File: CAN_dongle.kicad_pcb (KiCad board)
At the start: 2 copper layers, 70 x 70 mm, 77 parts, among them J1 P0-P3, J10 K-LINE, J11 HEADER2X10, J2 JTAG, J3 USB-MINI-A, J4 12V, J5 5V, J6 GND, J7 P4-P7, J8 CAN, J9 TERM, Q1 IRF7313, Q2 IRF7313, Q3 2N7002, Q4 2N7002, U1 LM324, U2 STM32F103CBT6, U3 LM1117, U4 MC34063, U5 MCP2551, X1 XT324

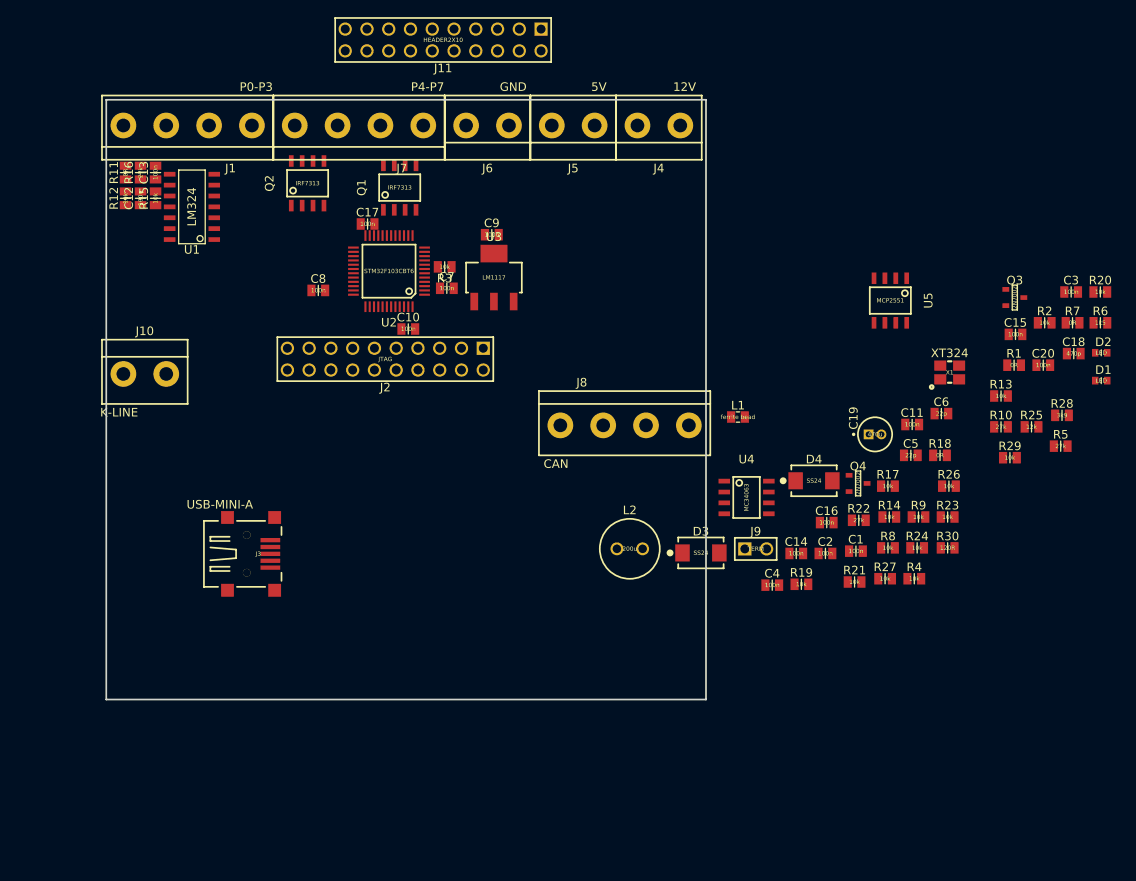
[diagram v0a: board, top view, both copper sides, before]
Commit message: Added LCD, buttons, remapped pins
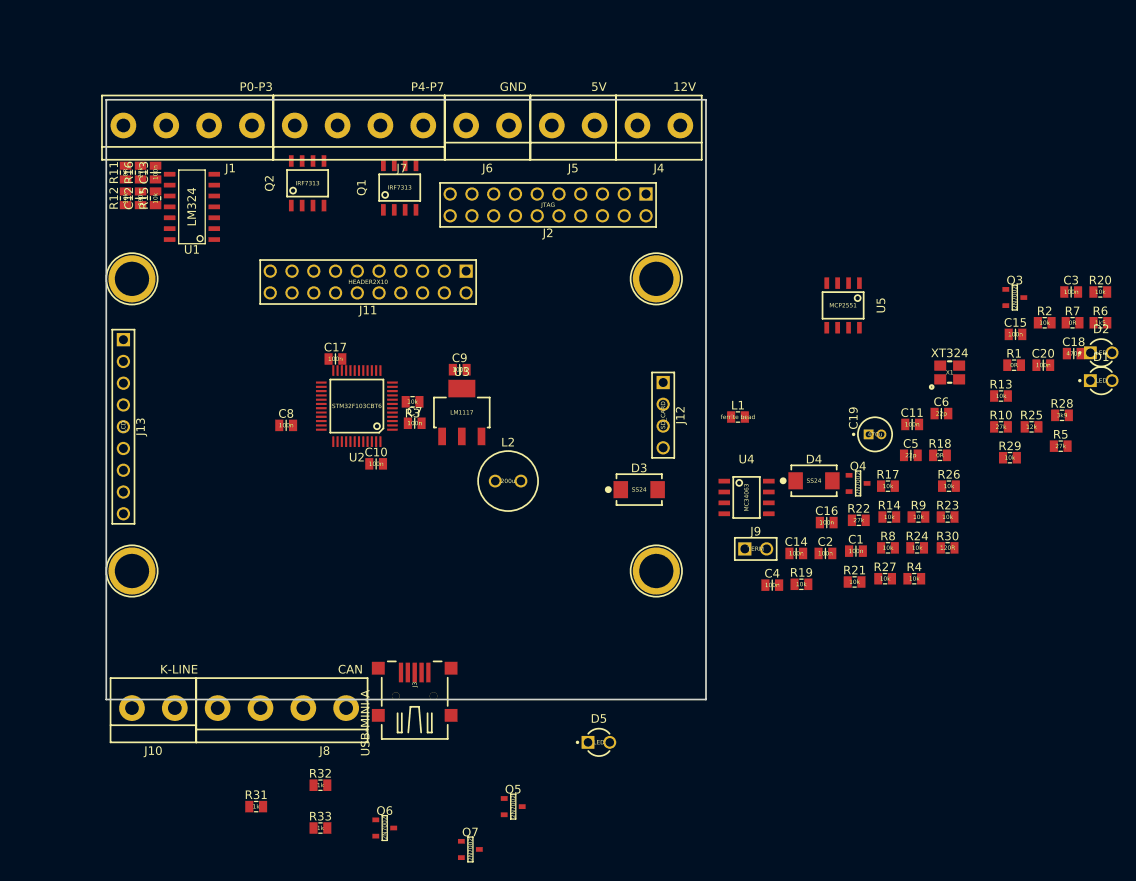
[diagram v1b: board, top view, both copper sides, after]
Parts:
- added D5: LED, z_newlib:LED_3MM, F.Cu at (137.5, 125.0)
- added J12: SD_CARD, z_pinHeaders:HEADER1x4V, F.Cu at (145.0, 83.0)
- added J13: LCD, z_pinHeaders:HEADER1x9V, F.Cu at (82.0, 78.0)
- added J14: LCD_MNTHOLE, z_newlib:MountHole_D4P6, F.Cu at (83.0, 105.0)
- added J15: LCD_MNTHOLE, z_newlib:MountHole_D4P6, F.Cu at (83.0, 70.9)
- added J16: LCD_MNTHOLE, z_newlib:MountHole_D4P6, F.Cu at (144.2, 70.9)
- added J17: LCD_MNTHOLE, z_newlib:MountHole_D4P6, F.Cu at (144.2, 105.0)
- added Q5: 2N7002, z_newlib:SOT23, F.Cu at (127.5, 132.5)
- added Q6: 2N7002, z_newlib:SOT23, F.Cu at (112.5, 135.0)
- added Q7: 2N7002, z_newlib:SOT23, F.Cu at (122.5, 137.5)
- added R31: 1k, z_newlib:R0805, F.Cu at (97.5, 132.5)
- added R32: 1k, z_newlib:R0805, F.Cu at (105.0, 130.0)
- added R33: 1k, z_newlib:R0805, F.Cu at (105.0, 135.0)
- D1, D2: footprint z_newlib:C0603 -> z_newlib:LED_3MM
- R1, R10, R11, R12, R13, R14, R15, R16, R17, R18, R19, R2, R20, R21, R22, R23, R24, R25, R26, R27, R28, R29, R3, R30, R4, R5, R6, R7, R8, R9: footprint z_newlib:C0805 -> z_newlib:R0805
- moved J8 41.4 mm to (108.0, 121.0), turned to 180 degrees
- moved J10 39.5 mm to (88.0, 121.0), turned to 180 degrees
- moved J3 33.3 mm to (116.0, 125.0), turned to 90 degrees
- moved J11 29.6 mm to (122.0, 70.0)
- moved J2 26.2 mm to (143.0, 61.0)
- moved L2 16.3 mm to (126.9, 94.5)
- moved C10 16.2 mm to (111.5, 92.5)
- moved C17 16.2 mm to (106.8, 80.2)
- moved C7 16.2 mm to (116.0, 87.8)
- moved C8 16.2 mm to (101.0, 88.0)
- moved C9 16.2 mm to (121.2, 81.5)
- moved R3 16.2 mm to (115.8, 85.2)
- moved U2 16.2 mm to (109.2, 85.8)
- moved U3 16.2 mm to (121.5, 86.5)
- moved D3 10.3 mm to (142.2, 95.5)
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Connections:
- D1 pad 1: /LED0 -> +3V3
- D1 pad 2: GND -> Net-(D1-Pad2)
- D2 pad 1: /LED1 -> +3V3
- D2 pad 2: GND -> Net-(D2-Pad2)
- J11 pad 2: +15V -> (no net)
- J2 pad 11: Net-(J2-Pad11) -> (no net)
- J2 pad 17: Net-(J2-Pad17) -> (no net)
- J2 pad 19: Net-(J2-Pad19) -> (no net)
- J3 pad 4: Net-(J3-Pad4) -> (no net)
- Q1 pad 2: /P5 -> /P9
- Q1 pad 4: /P4 -> /P8
- Q2 pad 2: /P7 -> /P11
- Q2 pad 4: /P6 -> /P10
- R13 pad 1: /P4 -> /P8
- R14 pad 1: /P5 -> /P9
- R17 pad 1: /P6 -> /P10
- R20 pad 1: /P7 -> /P11
- U2 pad 18: /P8 -> (no net)
- U2 pad 19: /P9 -> (no net)
- U2 pad 20: Net-(U2-Pad20) -> /LCD_D/C
- U2 pad 29: /LED0 -> /P8
- U2 pad 30: /LED1 -> /P9
- U2 pad 41: Net-(U2-Pad41) -> /LCD_LED
- U5 pad 5: Net-(U5-Pad5) -> (no net)

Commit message: Added calculator for ADC buttons. Added input for compression meter. First placement done.
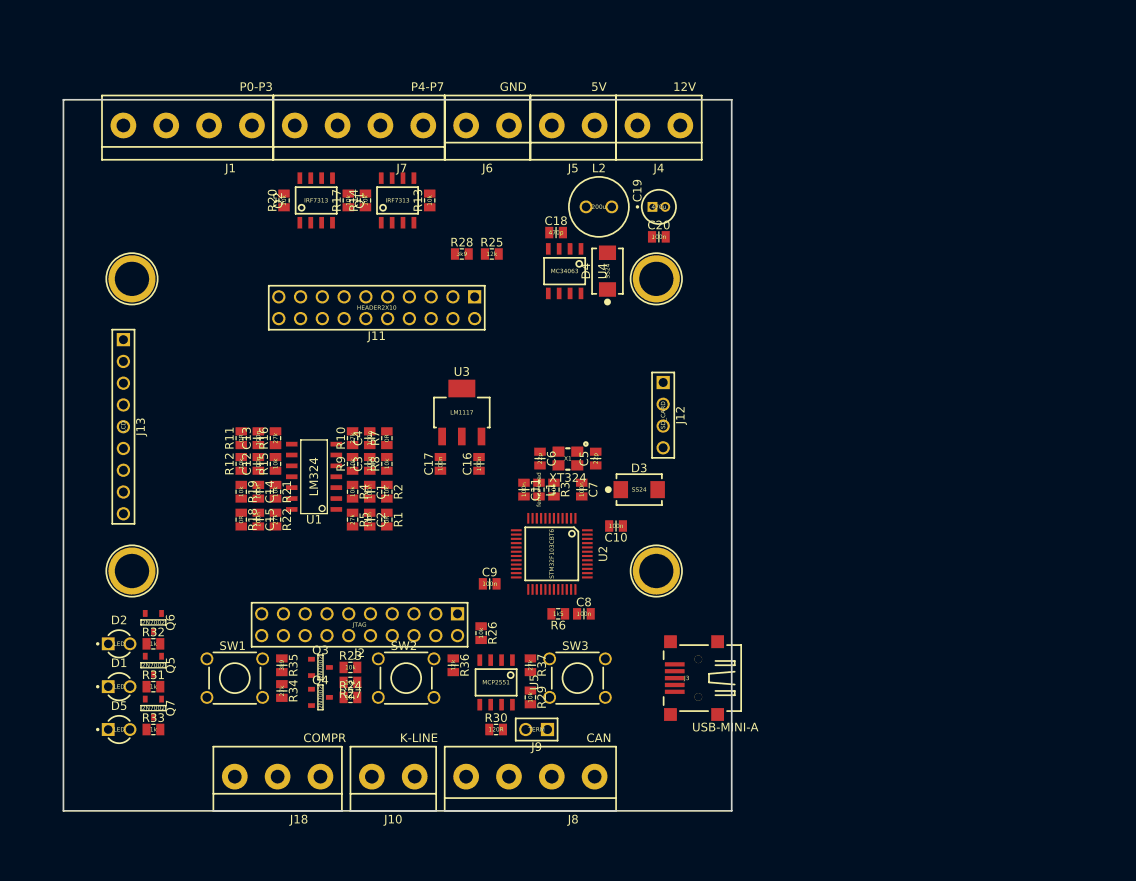
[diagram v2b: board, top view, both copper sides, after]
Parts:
- added J18: COMPR, z_pinHeaders:AK306_LE-3, F.Cu at (105.0, 129.0)
- added R34: 27k, z_newlib:C0805, F.Cu at (100.5, 119.0)
- added R35: 3k9, z_newlib:C0805, F.Cu at (100.5, 116.0)
- added R36: 12k, z_newlib:C0805, F.Cu at (120.5, 116.0)
- added R37: 27k, z_newlib:C0805, F.Cu at (129.5, 116.0)
- added SW1: SWITCH_DUALPINS, z_newlib:TACT_SWITCH_TH_5MM, F.Cu at (95.0, 117.5)
- added SW2: SWITCH_DUALPINS, z_newlib:TACT_SWITCH_TH_5MM, F.Cu at (115.0, 117.5)
- added SW3: SWITCH_DUALPINS, z_newlib:TACT_SWITCH_TH_5MM, F.Cu at (135.0, 117.5)
- moved D1 120.1 mm to (81.5, 118.5)
- moved D2 119.6 mm to (81.5, 113.5)
- moved R20 95.9 mm to (100.8, 61.8), turned to 90 degrees
- moved Q3 91.8 mm to (105.0, 116.2)
- moved C15 91.0 mm to (97.8, 99.0), turned to 270 degrees
- moved C3 84.3 mm to (110.8, 92.5), turned to 90 degrees
- moved R5 83.1 mm to (108.8, 99.0), turned to 270 degrees
- moved R18 81.9 mm to (95.8, 99.0), turned to 270 degrees
- moved R7 81.2 mm to (112.8, 89.5), turned to 90 degrees
- moved R2 79.3 mm to (112.8, 95.8), turned to 270 degrees
- moved R10 75.7 mm to (108.8, 89.5), turned to 90 degrees
- moved R1 75.4 mm to (112.8, 99.0), turned to 270 degrees
- moved R28 72.5 mm to (121.5, 68.0)
- moved R23 71.9 mm to (108.5, 116.2)
- moved R6 71.8 mm to (132.8, 110.0), turned to 180 degrees
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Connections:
- net Net-(J10-Pad2) renamed /K-LINE
- J11 pad 2: (no net) -> +12V
- J8 pad 1: GND -> +12V
- J8 pad 2: /CANL -> /CANH
- J8 pad 3: /CANH -> /CANL
- J8 pad 4: +12V -> GND
- U2 pad 18: (no net) -> /COMPRESSION
- U2 pad 19: (no net) -> /BUTTONS
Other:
- board size 70 x 70 mm -> 78 x 83 mm

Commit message: Finished first routing. Could be packed more. Verify LCD connectors placement. Reduce via sizes.
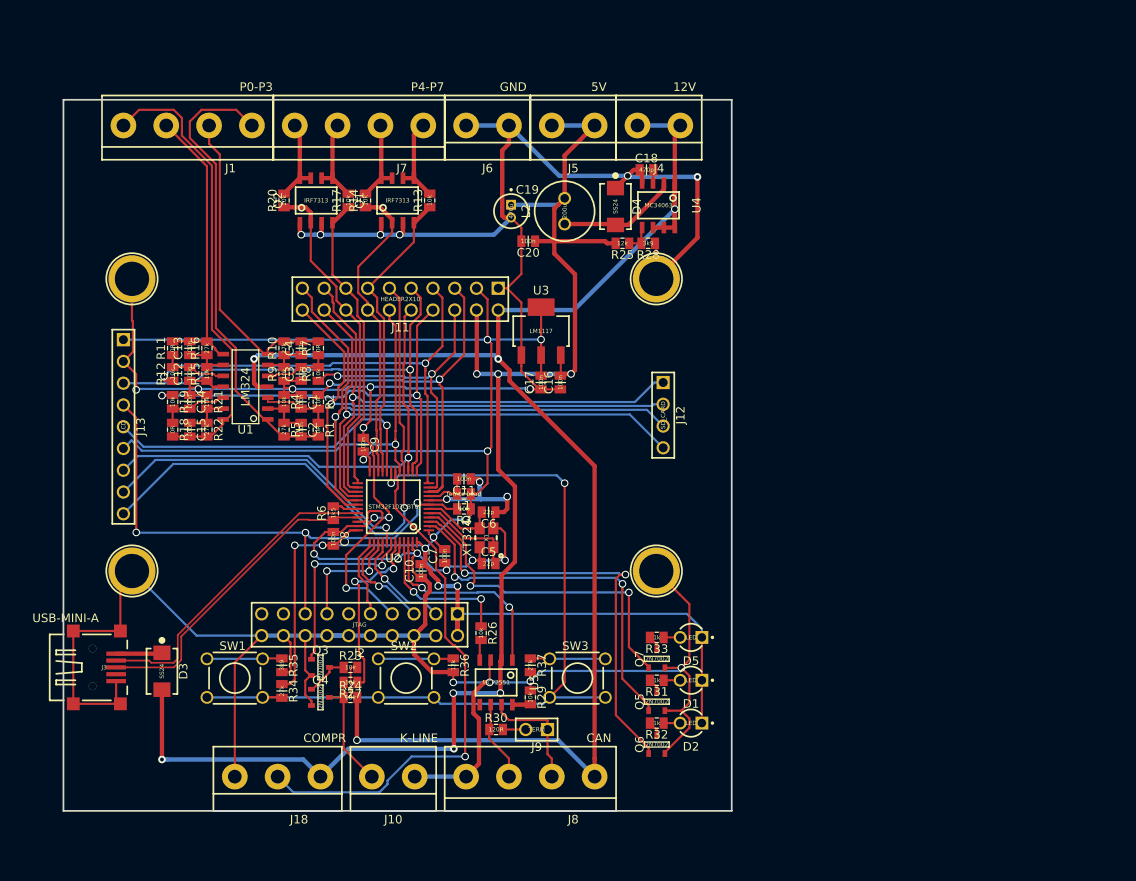
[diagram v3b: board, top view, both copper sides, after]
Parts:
- moved J3 81.5 mm to (73.0, 116.2), turned to 0 degrees
- moved D5 67.6 mm to (148.2, 112.8), turned to 180 degrees
- moved D2 67.4 mm to (148.2, 122.8), turned to 180 degrees
- moved D1 66.8 mm to (148.2, 117.8), turned to 180 degrees
- moved Q6 60.5 mm to (144.2, 125.2), turned to 90 degrees
- moved R33 59.7 mm to (144.2, 112.8), turned to 180 degrees
- moved D3 59.6 mm to (86.5, 116.7), turned to 270 degrees
- moved R32 59.5 mm to (144.2, 122.8), turned to 180 degrees
- moved Q7 59.0 mm to (144.2, 115.2), turned to 90 degrees
- moved Q5 58.9 mm to (144.2, 120.2), turned to 90 degrees
- moved R31 58.8 mm to (144.2, 117.8), turned to 180 degrees
- moved C8 30.5 mm to (106.5, 101.2), turned to 270 degrees
- moved R6 28.8 mm to (106.5, 98.2), turned to 90 degrees
- moved C10 23.3 mm to (116.8, 105.0), turned to 90 degrees
- moved C9 21.9 mm to (110.0, 90.2), turned to 270 degrees
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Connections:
- U2 pad 21: /P10 -> /P8
- U2 pad 22: /P11 -> /P9
- U2 pad 25: /P12 -> /P10
- U2 pad 26: /P13 -> /P11
- U2 pad 27: /P14 -> /P12
- U2 pad 28: /P15 -> /P13
- U2 pad 29: /P8 -> /P14
- U2 pad 30: /P9 -> /P15
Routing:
- net GND: track 0.00 -> 489.6 mm, vias 0 -> 27
- net +3V3: track 0.00 -> 210.0 mm, vias 0 -> 11
- net +12V: track 0.00 -> 182.5 mm, vias 0 -> 4
- net +5V: track 0.00 -> 170.7 mm, vias 0 -> 7
- net /BUTTONS: track 0.00 -> 97.5 mm, vias 0 -> 2
- net /P14: track 0.00 -> 69.1 mm, vias 0 -> 1
- net /P6: track 0.00 -> 67.4 mm, vias 0 -> 1
- net /P15: track 0.00 -> 66.8 mm, vias 0 -> 1
- net /NRST: track 0.00 -> 65.6 mm, vias 0 -> 3
- net /P12: track 0.00 -> 64.6 mm, vias 0 -> 1
- net /P13: track 0.00 -> 63.7 mm, vias 0 -> 1
- net /COMPRESSION: track 0.00 -> 61.6 mm, vias 0 -> 1
- net /P4: track 0.00 -> 57.1 mm, vias 0 -> 1
- net /P2: track 0.00 -> 56.9 mm, vias 0 -> 2
- net /P5: track 0.00 -> 54.3 mm, vias 0 -> 1
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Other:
- net class Default: clearance 0.254 -> 0.2032; trace_width 0.254 -> 0.2032
- rule trace_clearance: 0.254 -> 0.2032
- rule trace_min: 0.254 -> 0.2032

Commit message: Some optimisations. Moved LEDs to upper part of the board
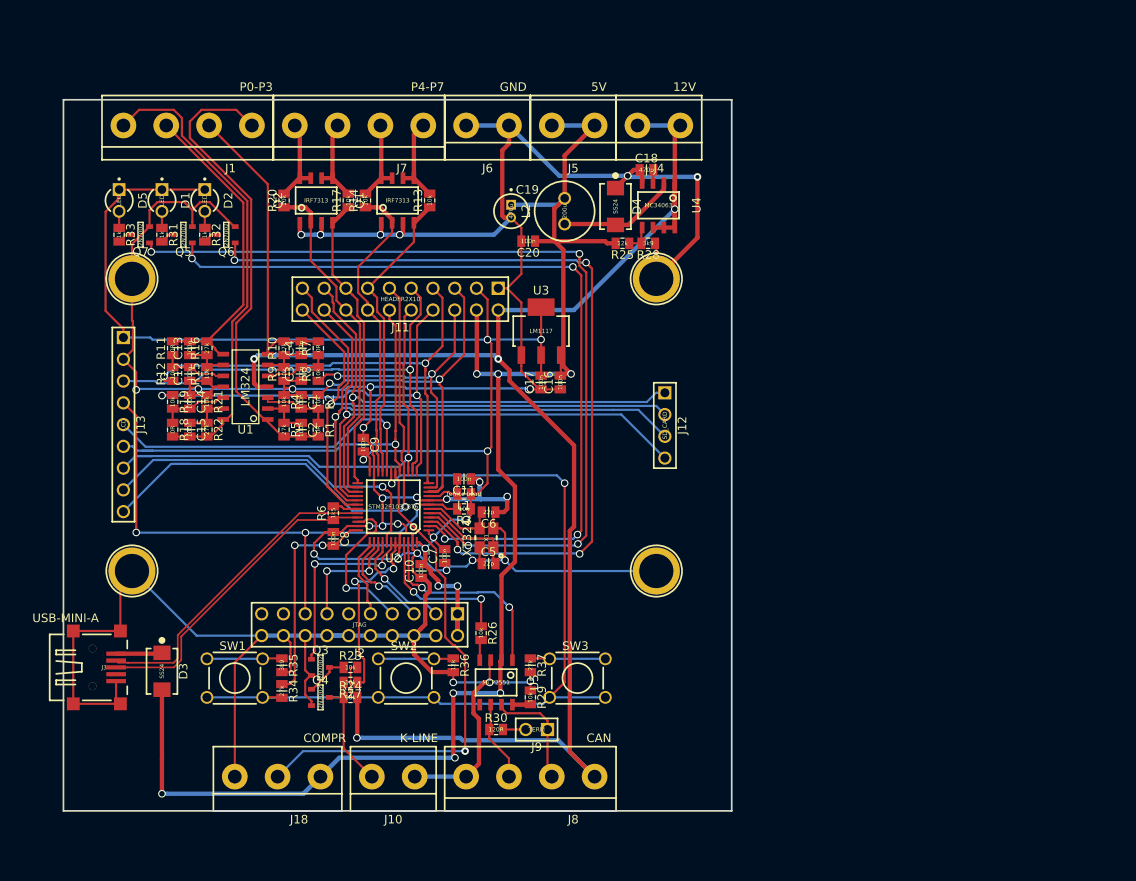
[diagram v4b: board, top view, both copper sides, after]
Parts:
- moved D5 84.0 mm to (81.5, 61.8), turned to 270 degrees
- moved D1 83.4 mm to (86.5, 61.8), turned to 270 degrees
- moved D2 83.3 mm to (91.5, 61.8), turned to 270 degrees
- moved R33 78.4 mm to (81.5, 65.8), turned to 270 degrees
- moved Q7 78.0 mm to (84.0, 65.8), turned to 180 degrees
- moved Q6 77.9 mm to (94.0, 65.8), turned to 180 degrees
- moved R31 77.7 mm to (86.5, 65.8), turned to 270 degrees
- moved R32 77.7 mm to (91.5, 65.8), turned to 270 degrees
- moved Q5 77.6 mm to (89.0, 65.8), turned to 180 degrees
- moved J12 1.22 mm to (145.2, 84.2)
- moved J13 0.25 mm to (82.0, 77.8)
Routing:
- net Net-(Q7-Pad1): track 39.6 -> 104.8 mm, vias 2 -> 4
- net Net-(Q5-Pad1): track 44.2 -> 97.1 mm, vias 2 -> 4
- net Net-(Q6-Pad1): track 50.4 -> 97.8 mm, vias 2 -> 4
- net +3V3: track 210.0 -> 198.6 mm
- net GND: track 489.6 -> 495.4 mm, vias 27 -> 29
- net +5V: track 170.7 -> 175.1 mm
- net /LCD_LED: track 37.2 -> 41.6 mm
- net Net-(C13-Pad2): track 33.8 -> 37.3 mm
- net /TMS: track 21.0 -> 18.4 mm
- net /COMPRESSION: track 61.6 -> 59.3 mm
- net /P5: track 54.3 -> 55.9 mm
- net Net-(C15-Pad2): track 53.3 -> 54.8 mm
- net Net-(C2-Pad2): track 54.2 -> 55.7 mm
- net /P6: track 67.4 -> 66.1 mm
- net /P14: track 69.1 -> 69.8 mm
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
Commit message: Added copper planes. Added some GND vias
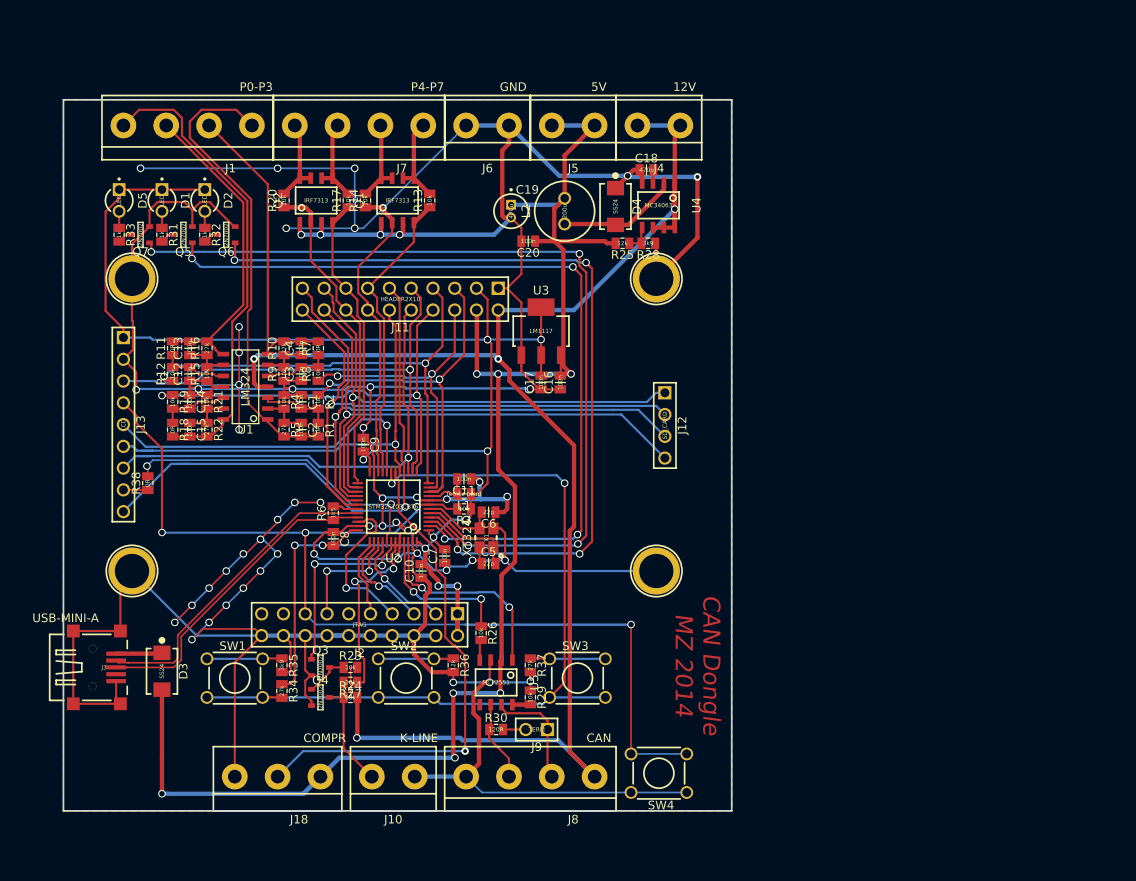
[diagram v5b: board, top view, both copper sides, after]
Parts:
- added R38: 0R, z_newlib:R0805, F.Cu at (84.9, 94.8)
- added SW4: SWITCH_DUALPINS, z_newlib:TACT_SWITCH_TH_5MM, F.Cu at (144.5, 128.6)
- R34, R35, R36, R37: footprint z_newlib:C0805 -> z_newlib:R0805
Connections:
- J13 pad 8: /LCD_LED -> Net-(J13-Pad8)
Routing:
- net GND: track 495.4 -> 647.2 mm, vias 29 -> 54
- net /NRST: track 65.5 -> 142.4 mm, vias 3 -> 4
- net /LCD_LED: track 41.6 -> 36.9 mm, vias 1 -> 2
- net Net-(J13-Pad8): track 0.00 -> 2.86 mm
- net Net-(C2-Pad2): track 55.7 -> 54.6 mm
- added copper zone on B.Cu, net GND
- added copper zone on F.Cu, net GND
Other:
- board text added: "CAN Dongle MZ 2014"
